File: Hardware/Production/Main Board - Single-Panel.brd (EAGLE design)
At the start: 86.4 x 73.7 mm, 88 parts, among them J1 MICROMOD-2222-C, J10 MICRO-SD-PUSH-PUSH-EXT-PIN, J2 Vertical Qwiic Connector, J4 QWIIC_RIGHT_ANGLE, J5 CORTEX_JTAG_DEBUG_MINIMUM_PTH, J6 MICROMOD_CARRIER, Q1 3.1A/30V/105mΩ, U2 MCP73831, U5 AP7361C-33

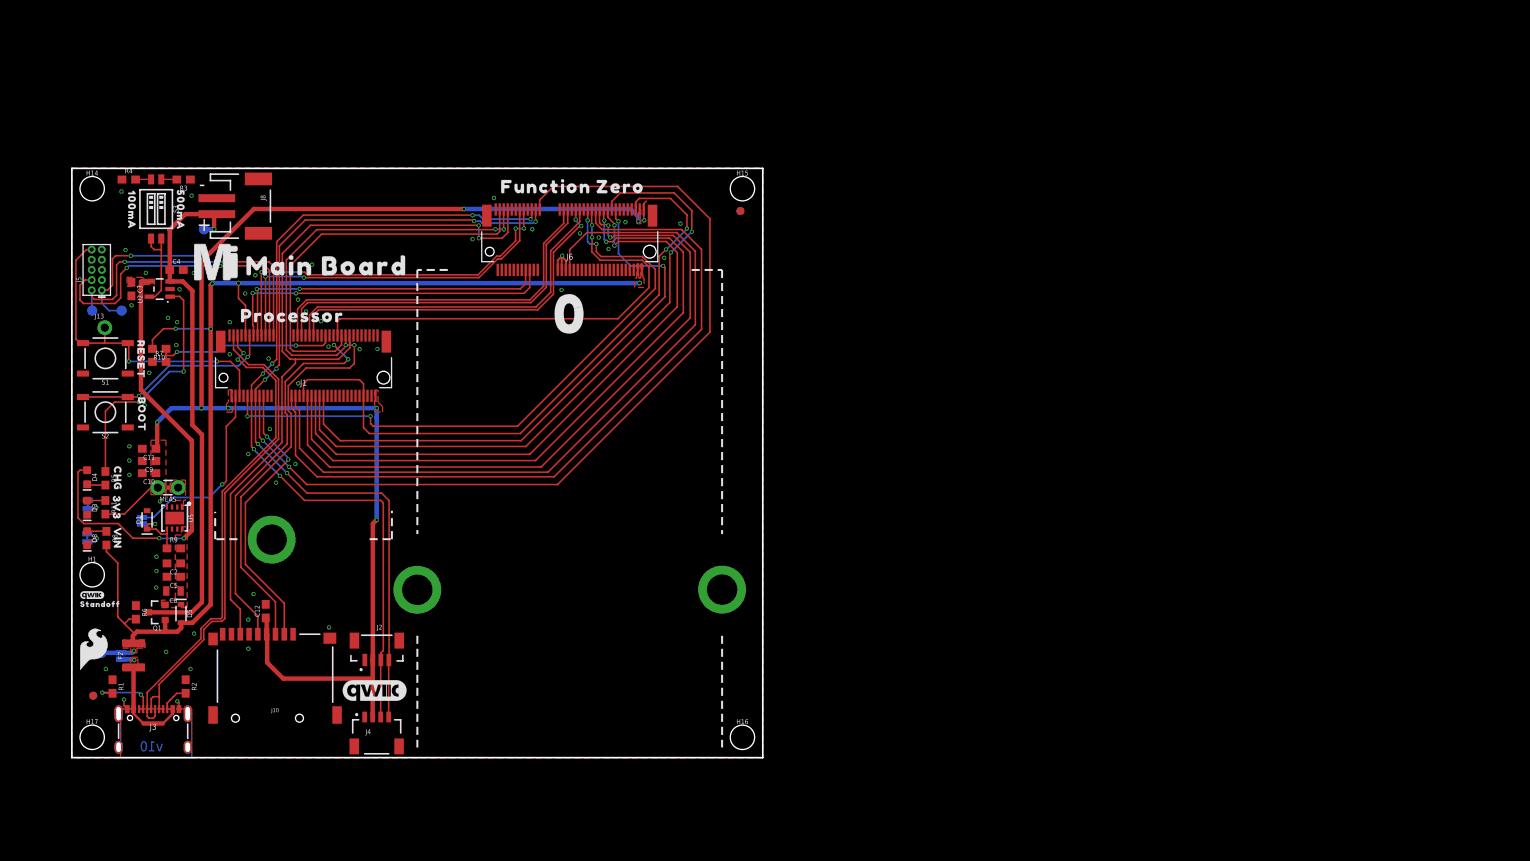
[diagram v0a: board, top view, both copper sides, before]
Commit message: Changes eagle file names
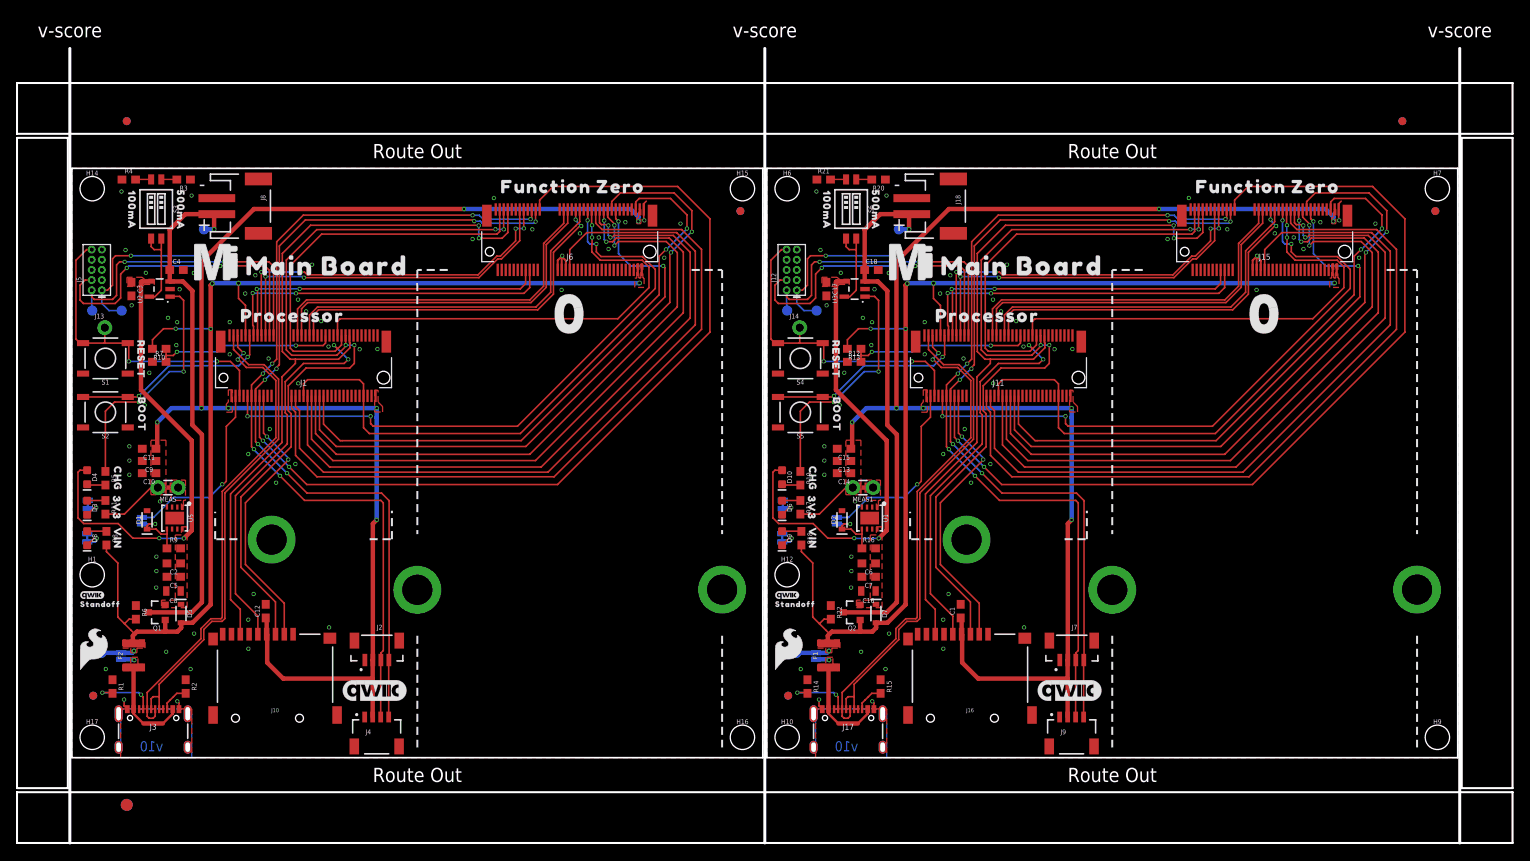
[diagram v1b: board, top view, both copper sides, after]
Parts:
- removed FRAME1: FRAME-LEDGER, SparkFun-Aesthetics:CREATIVE_COMMONS
- added 3V3_LED1, 5V_LED1: (no value), SparkFun-Jumpers:SMT-JUMPER_2_NC_TRACE_SILK
- added BYP1: JUMPER-SMT_2_NO_SILK, SparkFun-Jumpers:SMT-JUMPER_2_NO_SILK
- added C1, C14, C7: 0.1uF, SparkFun-Capacitors:0603
- added C13: 1.0uF, SparkFun-Capacitors:0603
- added C15, C6: 0.22uF, SparkFun-Capacitors:0603
- added C16: 10uF, SparkFun-Capacitors:0805
- added C17, C18: 4.7uF, SparkFun-Capacitors:0603
- added D10: Yellow, SparkFun-LED:LED-0603
- added D2: 3.3V, SparkFun-DiscreteSemi:SOD-323
- added D6, D9: RED, SparkFun-LED:LED-0603
- added D7: 3A/10V/280mV, SparkFun-DiscreteSemi:SOD-323
- added E$1, E$2, E$3, E$4: (no value), SparkFun-Aesthetics:FIDUCIAL-1X2
- added E$5, E$6: (no value), SparkFun-Retired:FIDUCIAL-1.5X3
- added F1: 6V/2A, SparkFun-Fuses:1210
- added FD5, FD6, FD7, FD8: FIDUCIAL1X2, SparkFun-Aesthetics:FIDUCIAL-1X2
- added H10, H12, H6, H7, H9: STAND-OFFTIGHT, SparkFun-Hardware:STAND-OFF-TIGHT
- added H11, H2, H5: STAND-OFF-REFLOW-M2.5_2.5MM_TALL, SparkFun-Hardware:STAND-OFF-REFLOW-M2.5
- added J11: MICROMOD-2222-C, SparkFun-MicroMod:M.2-CONNECTOR-E
- added J12: CORTEX_JTAG_DEBUG_MINIMUM_PTH, SparkFun-Connectors:2X5-PTH-1.27MM
- added J14: (no value), SparkFun-Connectors:1X01_NO_SILK
- added J15: MICROMOD_CARRIER, SparkFun-MicroMod-Function:M.2-CONNECTOR-E-FUNCTION-STANDARD
- added J16: MICRO-SD-PUSH-PUSH-EXT-PIN, SparkFun-Connectors:MICROSD-EXTERNALPIN
- added J17: (no value), SparkFun-Connectors:USB-C-16P-2LAYER-PADS
- added J18: (no value), SparkFun-Connectors:JST-2-SMD
- added J7: Vertical Qwiic Connector, SparkFun-Connectors:JST04_1MM_VERT
- added J9: QWIIC_RIGHT_ANGLE, SparkFun-Connectors:JST04_1MM_RA
- added LOGO4: QWIIC_LOGO_8MM, SparkFun-Aesthetics:QWIIC_8MM
- added LOGO5: SFE_LOGO_NAME_FLAME.3_INCH, SparkFun-Aesthetics:SFE_LOGO_NAME_FLAME_.3
- added LOGO6: OSHW-LOGOL, SparkFun-Aesthetics:OSHW-LOGO-L
- added MEAS1: JUMPER-COMBO_2_NC_TRACE, SparkFun-Jumpers:COMBO-JUMPER_2_NC_TRACE
- added Q2: 3.1A/30V/105mΩ, SparkFun-DiscreteSemi:SOT23-3
- added R12, R21, R22: 10k, SparkFun-Resistors:0603
- added R13: 20k, SparkFun-Resistors:0603
- added R14, R15: 5.1k, SparkFun-Resistors:0603
- added R16: 100k, SparkFun-Resistors:0603
- added R17, R19: 1k, SparkFun-Resistors:0603
- added R18: 4.7k, SparkFun-Resistors:0603
- added R20: 2.0k, SparkFun-Resistors:0603
- added S4: Reset, SparkFun-Switches:TACTILE_SWITCH_SMD_5.2MM
- added S5: BOOT, SparkFun-Switches:TACTILE_SWITCH_SMD_5.2MM
- added S6: DIP-02-SMD-50MIL, SparkFun-Switches:DIPSWITCH-02-50MIL
- added TP5, TP6, TP7, TP8: TEST-POINT3X5, SparkFun-Connectors:PAD.03X.05
- added U$23: (no value), top:3V332530
- added U$24: (no value), top:VIN32529
- added U$25: (no value), top:CHG32528
- added U$26: (no value), top:FUNCTION_ZERO517
- added U$27: (no value), top:PROCESSOR522
- added U$28: (no value), top:#3V3_LED#17
- added U$29: (no value), top:#VIN_LED#16
- added U$30: (no value), top:#PTC#18
- added U$31: (no value), top:BOOT32541
- added U$32: (no value), top:RESET32540
- added U$33: (no value), top:#3V3_EN#18
- added U$34: (no value), SparkFun-MicroMod:MICROMOD_MI_LOGO_1
- added U$35: (no value), top:0525
- added U$36: (no value), top:MAIN523
- added U$37: (no value), top:BOARD524
- added U$38: (no value), top:100MA6
- added U$39: (no value), top:500MA101
- added U$40: (no value), top:MAIN_BOARD5523
- added U$41: (no value), SparkFun-MicroMod:MICROMOD_LOGO_1
- added U$42: (no value), SparkFun-Aesthetics:QWIIC_3MM
- added U$43: (no value), top:STANDOFF501
- added U$44: (no value), SparkFun-Aesthetics:SFE_LOGO_FLAME_.2
- added U1: AP7361C-33, SparkFun-IC-Power:UDFN-8
- added U3: MCP73831, SparkFun-IC-Power:SOT23-5
- added VE1: (no value), SparkFun-Jumpers:SMT-JUMPER_2_NO_SILK
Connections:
- new net !BOOT!1: J11.11, S5.3, S5.4
- new net !CS0!-PROCESSOR1: J11.55, J15.49
- new net !RESET!1: J11.6, J12.10, J14.1, S4.3, S4.4
- new net 3.3V1: C1.1, C13.1, C14.1, C15.1, J11.2, J11.74, J12.1, J15.73, J16.4, J7.2, J9.2, MEAS1.2, MEAS1.4, R17.2, TP5.1
- new net 3.3V_EN1: J11.4, VE1.1
- new net 3.3V_EN_VE1: D2.C, R16.1, U1.5, VE1.2
- new net A0-PROCESSOR1: J11.34, J15.38
- new net CTS1-PROCESSOR1: J11.15, J15.16
- new net D+1: J11.3, J17.A6, J17.B6
- new net D-1: J11.5, J17.A7, J17.B7
- new net D0-PROCESSOR1: J11.10, J15.47
- new net D1-PROCESSOR/SD_CARD_!CS!1: J11.18, J16.2
- new net G0-PROCESSOR1: J11.40, J15.53
- new net G1-PROCESSOR1: J11.42, J15.55
- new net G2-PROCESSOR1: J11.44, J15.57
- new net G3-PROCESSOR1: J11.46, J15.59
- new net G4-PROCESSOR1: J11.48, J15.61
- new net GND1: 3V3_LED1.1, 5V_LED1.1, C1.2, C13.2, C14.2, C15.2, C16.2, C17.2, C18.2, C6.2, C7.2, D2.A, H11.1, H2.1, H5.1, J11.1, J11.33, J11.36, J11.39, J11.45, J11.7, J11.75, J12.3, J12.5, J12.9, J15.1, J15.32, J15.33, J15.34, J15.36, J15.39, J15.45, J15.75, J16.10, J16.11, J16.12, J16.13, J16.6, J17.GND, J17.GND2, J18.1, J7.1, J9.1, R12.1, R14.1, R15.1, R20.1, R21.1, R22.1, S4.1, S4.2, S5.1, S5.2, U1.4, U1.EP, U3.2
- new net HOST_D+1: J11.35, J15.35
- new net HOST_D-1: J11.37, J15.37
- new net I2C_!INT!1: J11.16, J15.23
- new net I2C_SCL1: J11.14, J15.21, J7.4, J9.4
- new net I2C_SDA1: J11.12, J15.19, J7.3, J9.3
- new net N$1: J17.B5, R15.2
- new net N$13: J17.A5, R14.2
- new net N$16: MEAS1.1, MEAS1.3, U1.1
- new net N$17: D6.A, R17.1
- new net N$18: BYP1.1, F1.1, J17.VBUS1, J17.VBUS2
- new net N$19: D9.A, R18.1
- new net N$20: 5V_LED1.2, D9.C
- new net N$21: 3V3_LED1.2, D6.C
- new net N$22: S6.3, S6.4, U3.5
- new net N$23: D10.C, R19.2
- new net N$24: R19.1, U3.1
- new net N$25: R20.2, S6.1
- new net N$26: R21.2, S6.2
- new net PROCESSOR_CAN-RX1: J11.41, J15.43
- new net PROCESSOR_CAN-TX1: J11.43, J15.41
- new net PWM0-PROCESSOR1: J11.32, J15.51
- new net PWR_EN1: J11.38, J11.68, J15.71
- new net RTS1-PROCESSOR1: J11.13, J15.18
- new net RX1-PROCESSOR1: J11.19, J15.13
- new net SPI_PROCESSOR_SCK1: J11.57, J15.3, J16.5
- new net SPI_PROCESSOR_SDI1: J11.61, J15.7, J16.7
- new net SPI_PROCESSOR_SDO1: J11.59, J15.5, J16.3
- new net SWDCK1: J11.21, J12.4
- new net SWDIO1: J11.23, J12.2, TP8.1
- new net TX1-PROCESSOR1: J11.17, J15.15
- new net VCC1: C16.1, C17.1, C6.1, C7.1, D10.A, D7.C, Q2.2, R16.2, U1.8, U3.4
- new net VIN/1: J11.49, R12.2, R13.1
- new net VIN1: BYP1.2, D7.A, F1.2, J11.9, J15.72, J15.74, Q2.1, R13.2, R18.2, R22.2, TP7.1
- new net V_BATT1: C18.1, J18.2, Q2.3, TP6.1, U3.3
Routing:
- net 3.3V1: track 0.00 -> 195.7 mm, vias 0 -> 9
- net VIN1: track 0.00 -> 142.2 mm, vias 0 -> 6
- net I2C_!INT!1: track 0.00 -> 110.8 mm, vias 0 -> 2
- net I2C_SDA1: track 0.00 -> 107.9 mm, vias 0 -> 6
- net I2C_SCL1: track 0.00 -> 107.7 mm, vias 0 -> 6
- net SPI_PROCESSOR_SDO1: track 0.00 -> 100.4 mm, vias 0 -> 4
- net SPI_PROCESSOR_SCK1: track 0.00 -> 96.8 mm, vias 0 -> 2
- net SPI_PROCESSOR_SDI1: track 0.00 -> 95.9 mm, vias 0 -> 2
- net A0-PROCESSOR1: track 0.00 -> 94.4 mm
- net PWM0-PROCESSOR1: track 0.00 -> 93.4 mm
- net G0-PROCESSOR1: track 0.00 -> 86.5 mm, vias 0 -> 2
- net G1-PROCESSOR1: track 0.00 -> 83.0 mm, vias 0 -> 2
- net G3-PROCESSOR1: track 0.00 -> 81.4 mm, vias 0 -> 2
- net PWR_EN1: track 0.00 -> 79.2 mm, vias 0 -> 2
- net G2-PROCESSOR1: track 0.00 -> 78.9 mm, vias 0 -> 2
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- added copper zone on layer 1, net 3.3V1
- added copper zone on layer 1, net GND1
- added copper zone on layer 16, net GND1
- added copper zone on layer 1, net N$16
- added copper zone on layer 1, net N$18
- added copper zone on layer 1, net SHLD1
- added copper zone on layer 16, net SHLD1
- added copper zone on layer 1, net VCC1
- added copper zone on layer 1, net VIN1
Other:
- board size 86.4 x 73.7 mm -> 186.9 x 99.3 mm
- board text added: "Route Out"
- board text added: "v-score"
- board text removed: "Elias Santistevan"
- board text removed: "Units in Inches"
